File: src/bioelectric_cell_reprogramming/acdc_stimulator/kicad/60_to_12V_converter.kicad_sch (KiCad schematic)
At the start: 7 parts, among them IC4 LTC3637IMSE#PBF

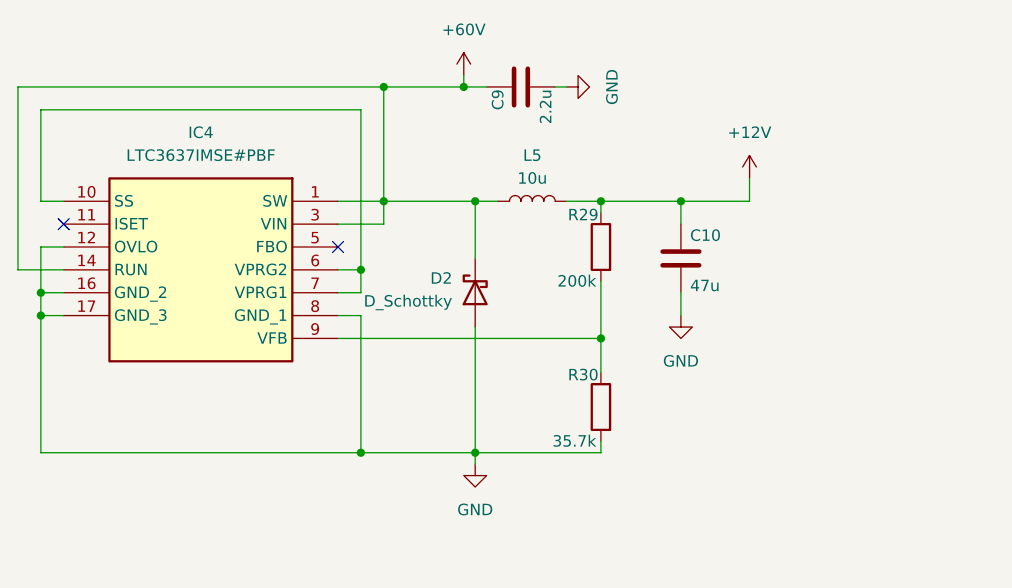
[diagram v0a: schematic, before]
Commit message: CI: footprint assignment done
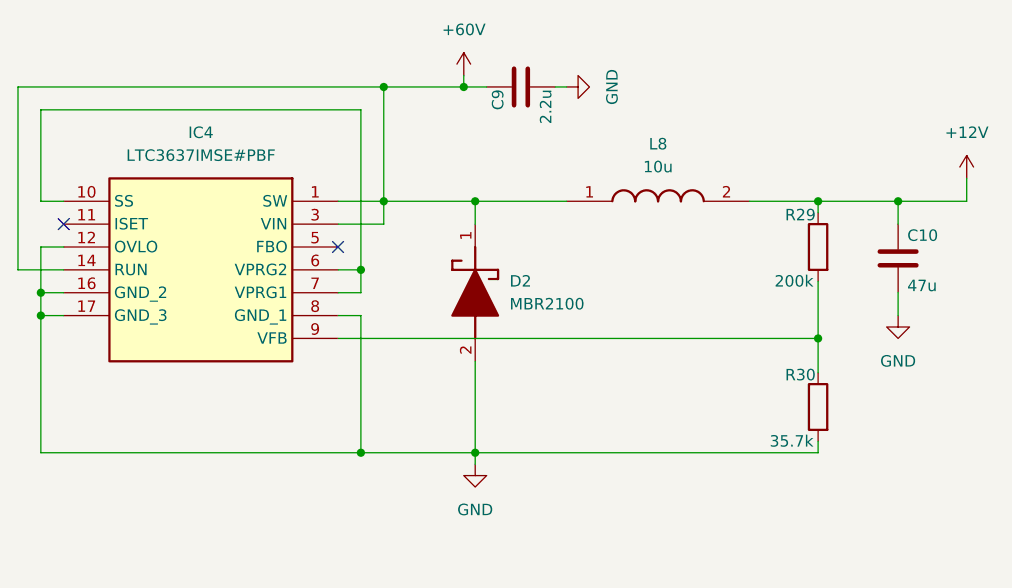
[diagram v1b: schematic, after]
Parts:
- removed D2: D_Schottky, symbol Device:D_Schottky
- removed L5: 10u, symbol Device:L
- added D2: MBR2100, MBR2100:DIOAD1910W86L670D310, symbol MBR2100:MBR2100
- added L8: 10u, SRP1270-100M:INDPM137137X700N, symbol SRP1270-100M:SRP1270-100M
- C10: footprint (none) -> Capacitor_SMD:C_0805_2012Metric
- C9: footprint (none) -> Capacitor_SMD:C_0603_1608Metric
- IC4: footprint LTC3637IMSEPBF -> LTC3637IMSE#PBF:LTC3637IMSEPBF
- R29: footprint (none) -> Resistor_SMD:R_0603_1608Metric
- R30: footprint (none) -> Resistor_SMD:R_0402_1005Metric
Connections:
- net +12V: now also L8.2
- net +60V: now also D2.1 (K), L8.1
- net GND: now also D2.2 (A)
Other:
- moved on the sheet: C10, R29, R30

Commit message: ci: STM32 layout done and schematic annotated
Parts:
- renumbered C9 to C53, C10 to C54, L8 to L5, R29 to R28, R30 to R29
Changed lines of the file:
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@@
 		(dnp no)
 		(fields_autoplaced yes)
-		(property "Reference" "#PWR081"
+		(property "Reference" "#PWR086"
 			(at 179.07 72.39 0)
 			(effects
@@
 			(project "acdc_stimulator"
 				(path "/ec70e9f6-566f-44ea-8141-5580f51beca4/cf0126de-2a37-4fca-bf65-f8dc79cc90bd"
-					(reference "#PWR081")
+					(reference "#PWR086")
 					(unit 1)
 				)
@@
 		(dnp no)
 		(fields_autoplaced yes)
-		(property "Reference" "L8"
+		(property "Reference" "L5"
 			(at 182.88 78.74 0)
 			(effects
@@
 			(project ""
 				(path "/ec70e9f6-566f-44ea-8141-5580f51beca4/cf0126de-2a37-4fca-bf65-f8dc79cc90bd"
-					(reference "L8")
+					(reference "L5")
 					(unit 1)
 				)
@@
 		(on_board yes)
 		(dnp no)
-		(property "Reference" "R30"
+		(property "Reference" "R29"
 			(at 200.406 104.394 0)
 			(effects
@@
 			(project "acdc_stimulator"
 				(path "/ec70e9f6-566f-44ea-8141-5580f51beca4/cf0126de-2a37-4fca-bf65-f8dc79cc90bd"
-					(reference "R30")
+					(reference "R29")
 					(unit 1)
 				)
@@
 		(dnp no)
 		(fields_autoplaced yes)
-		(property "Reference" "#PWR025"
+		(property "Reference" "#PWR084"
 			(at 161.29 74.93 0)
 			(effects
@@
 			(project "acdc_stimulator"
 				(path "/ec70e9f6-566f-44ea-8141-5580f51beca4/cf0126de-2a37-4fca-bf65-f8dc79cc90bd"
-					(reference "#PWR025")
+					(reference "#PWR084")
 					(unit 1)
 				)
@@
 		(on_board yes)
 		(dnp no)
-		(property "Reference" "C10"
+		(property "Reference" "C54"
 			(at 210.566 88.9 0)
 			(effects
@@
 			(project "acdc_stimulator"
 				(path "/ec70e9f6-566f-44ea-8141-5580f51beca4/cf0126de-2a37-4fca-bf65-f8dc79cc90bd"
-					(reference "C10")
+					(reference "C54")
 					(unit 1)
 				)
@@
 		(dnp no)
 		(fields_autoplaced yes)
-		(property "Reference" "#PWR082"
+		(property "Reference" "#PWR087"
 			(at 209.55 104.14 0)
 			(effects
@@
 			(project "acdc_stimulator"
 				(path "/ec70e9f6-566f-44ea-8141-5580f51beca4/cf0126de-2a37-4fca-bf65-f8dc79cc90bd"
-					(reference "#PWR082")
+					(reference "#PWR087")
 					(unit 1)
 				)
@@
 		(on_board yes)
 		(dnp no)
-		(property "Reference" "C9"
+		(property "Reference" "C53"
 			(at 165.1 72.644 0)
 			(effects
@@
 			(project "acdc_stimulator"
 				(path "/ec70e9f6-566f-44ea-8141-5580f51beca4/cf0126de-2a37-4fca-bf65-f8dc79cc90bd"
-					(reference "C9")
+					(reference "C53")
 					(unit 1)
 				)
@@
 		(dnp no)
 		(fields_autoplaced yes)
-		(property "Reference" "#PWR083"
+		(property "Reference" "#PWR088"
 			(at 217.17 86.36 0)
 			(effects
@@
 			(project "acdc_stimulator"
 				(path "/ec70e9f6-566f-44ea-8141-5580f51beca4/cf0126de-2a37-4fca-bf65-f8dc79cc90bd"
-					(reference "#PWR083")
+					(reference "#PWR088")
 					(unit 1)
 				)
@@
 		(on_board yes)
 		(dnp no)
-		(property "Reference" "R29"
+		(property "Reference" "R28"
 			(at 200.406 86.614 0)
 			(effects
@@
 			(project "acdc_stimulator"
 				(path "/ec70e9f6-566f-44ea-8141-5580f51beca4/cf0126de-2a37-4fca-bf65-f8dc79cc90bd"
-					(reference "R29")
+					(reference "R28")
 					(unit 1)
 				)
@@
 		(dnp no)
 		(fields_autoplaced yes)
-		(property "Reference" "#PWR080"
+		(property "Reference" "#PWR085"
 			(at 162.56 120.65 0)
 			(effects
@@
 			(project "acdc_stimulator"
 				(path "/ec70e9f6-566f-44ea-8141-5580f51beca4/cf0126de-2a37-4fca-bf65-f8dc79cc90bd"
-					(reference "#PWR080")
-					(unit 1)
-				)
+					(reference "#PWR085")
+					(unit 1)
+				)

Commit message: ci: layout done
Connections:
- net +60V: no longer D2.1 (K), IC4.1 (SW), L5.1
- new net: D2.1 (K), IC4.1 (SW), L5.1
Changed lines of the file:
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@@
 	(paper "A4")
 	(junction
+		(at 152.4 72.39)
+		(diameter 0)
+		(color 0 0 0 0)
+	)
+	(junction
 		(at 149.86 92.71)
 		(diameter 0)
@@
 	)
 	(junction
-		(at 152.4 72.39)
-		(diameter 0)
-		(color 0 0 0 0)
-	)
-	(junction
 		(at 200.66 100.33)
-		(diameter 0)
-		(color 0 0 0 0)
-	)
-	(junction
-		(at 152.4 85.09)
 		(diameter 0)
 		(color 0 0 0 0)
@@
 	(wire
 		(pts
-			(xy 152.4 85.09) (xy 147.32 85.09)
+			(xy 147.32 85.09) (xy 162.56 85.09)
 		)
 		(stroke
@@
 	(wire
 		(pts
-			(xy 161.29 72.39) (xy 152.4 72.39)
-		)
-		(stroke
-			(width 0)
-			(type default)
-		)
-	)
-	(wire
-		(pts
 			(xy 147.32 97.79) (xy 149.86 97.79)
 		)
@@
 	(wire
 		(pts
-			(xy 152.4 85.09) (xy 152.4 87.63)
-		)
-		(stroke
-			(width 0)
-			(type default)
-		)
-	)
-	(wire
-		(pts
 			(xy 114.3 95.25) (xy 114.3 90.17)
 		)
@@
 	(wire
 		(pts
-			(xy 152.4 85.09) (xy 162.56 85.09)
+			(xy 152.4 72.39) (xy 152.4 87.63)
 		)
 		(stroke
@@
 	(wire
 		(pts
+			(xy 152.4 72.39) (xy 161.29 72.39)
+		)
+		(stroke
+			(width 0)
+			(type default)
+		)
+	)
+	(wire
+		(pts
 			(xy 193.04 85.09) (xy 200.66 85.09)
 		)
@@
 		)
 		(stroke
-			(width 0)
-			(type default)
-		)
-	)
-	(wire
-		(pts
-			(xy 152.4 72.39) (xy 152.4 85.09)
-		)
-		(stroke

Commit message: BOM in progress
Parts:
- C53: Distributor Link (none) -> https://jlcpcb.com/partdetail/3409988-GRM21BD72A225KE01L/C2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; Manufacturer (none) -> Murata Electronics; Manufacturer Part Number (none) -> GRM21BD72A225KE01L
- C54: footprint Capacitor_SMD:C_0805_2012Metric -> Capacitor_SMD:C_1206_3216Metric; Distributor Link (none) -> https://jlcpcb.com/partdetail/183737-1206X476M160NT/C172351; Manufacturer (none) -> FH (Guangdong Fenghua Advanced Tech); Manufacturer Part Number (none) -> 1206X476M160NT
- D2: Distributor Link (none) -> https://www.digikey.com/en/products/detail/panjit-internati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; Manufacturer (none) -> Panjit International Inc.; Manufacturer Part Number (none) -> MBR2100_R2_00001
- IC4: Distributor Link (none) -> https://jlcpcb.com/partdetail/AnalogDevices-LTC3637IMSEPBF/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; Manufacturer (none) -> Analog Devices; Manufacturer Part Number (none) -> LTC3637IMSE#PBF
- L5: Distributor Link (none) -> https://www.mouser.com/ProductDetail/Bourns/SRP1270-100M?qs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; Manufacturer (none) -> Bourns; Manufacturer Part Number (none) -> SRP1270-100M
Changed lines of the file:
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@@
 			)
 		)
-		(property "Distributor Link" ""
+		(property "Distributor Link" "https://www.digikey.com/en/products/detail/panjit-international-inc/MBR2100-R2-00001/15801106"
 			(at 162.56 85.09 0)
 			(effects
@@
 			)
 		)
-		(property "Manufacturer" ""
+		(property "Manufacturer" "Panjit International Inc."
 			(at 162.56 85.09 0)
 			(effects
@@
 			)
 		)
-		(property "Manufacturer Part Number" ""
+		(property "Manufacturer Part Number" "MBR2100_R2_00001"
+			(at 162.56 85.09 0)
+			(effects
+				(font
+					(size 1.27 1.27)
+				)
+				(hide yes)
+			)
+		)
+		(property "JLCPCB Part #" ""
 			(at 162.56 85.09 0)
 			(effects
@@
 			)
 		)
-		(property "Distributor Link" ""
+		(property "Distributor Link" "https://www.mouser.com/ProductDetail/Bourns/SRP1270-100M?qs=s%252BX%2FYkvGCpE5rFNaoMUDIw%3D%3D"
 			(at 172.72 85.09 0)
 			(effects
@@
 			)
 		)
-		(property "Manufacturer" ""
+		(property "Manufacturer" "Bourns"
 			(at 172.72 85.09 0)
 			(effects
@@
 			)
 		)
-		(property "Manufacturer Part Number" ""
+		(property "Manufacturer Part Number" "SRP1270-100M"
+			(at 172.72 85.09 0)
+			(effects
+				(font
+					(size 1.27 1.27)
+				)
+				(hide yes)
+			)
+		)
+		(property "JLCPCB Part #" ""
 			(at 172.72 85.09 0)
 			(effects
@@
 			)
 		)
+		(property "JLCPCB Part #" ""
+			(at 200.66 107.95 0)
+			(effects
+				(font
+					(size 1.27 1.27)
+				)
+				(hide yes)
+			)
+		)
 		(pin "1"
 		)
@@
 			)
 		)
-		(property "Footprint" "Capacitor_SMD:C_0805_2012Metric"
+		(property "Footprint" "Capacitor_SMD:C_1206_3216Metric"
 			(at 210.5152 95.25 0)
 			(effects
@@
 			)
 		)
-		(property "Distributor Link" ""
+		(property "Distributor Link" "https://jlcpcb.com/partdetail/183737-1206X476M160NT/C172351"
 			(at 209.55 91.44 0)
 			(effects
@@
 			)
 		)
-		(property "Manufacturer" ""
+		(property "Manufacturer" "FH (Guangdong Fenghua Advanced Tech)"
 			(at 209.55 91.44 0)
 			(effects
@@
 			)
 		)
-		(property "Manufacturer Part Number" ""
+		(property "Manufacturer Part Number" "1206X476M160NT"
+			(at 209.55 91.44 0)
+			(effects
+				(font
+					(size 1.27 1.27)
+				)
+				(hide yes)
+			)
+		)
+		(property "JLCPCB Part #" ""
 			(at 209.55 91.44 0)
 			(effects
@@
 			)
 		)
-		(property "Distributor Link" ""
+		(property "Distributor Link" "https://jlcpcb.com/partdetail/AnalogDevices-LTC3637IMSEPBF/C580783"
 			(at 147.32 85.09 0)
 			(effects
@@
 			)
 		)
-		(property "Manufacturer" ""
+		(property "Manufacturer" "Analog Devices"
 			(at 147.32 85.09 0)
 			(effects
@@
 			)
 		)
-		(property "Manufacturer Part Number" ""
+		(property "Manufacturer Part Number" "LTC3637IMSE#PBF"
+			(at 147.32 85.09 0)
+			(effects
+				(font
+					(size 1.27 1.27)
+				)
+				(hide yes)
+			)
+		)
+		(property "JLCPCB Part #" ""
 			(at 147.32 85.09 0)
 			(effects
@@
 			)
 		)
-		(property "Distributor Link" ""
+		(property "Distributor Link" "https://jlcpcb.com/partdetail/3409988-GRM21BD72A225KE01L/C2981733"
 			(at 167.64 72.39 0)
 			(effects
@@
 			)
 		)
-		(property "Manufacturer" ""
+		(property "Manufacturer" " Murata Electronics"
 			(at 167.64 72.39 0)
 			(effects
@@
 			)
 		)
-		(property "Manufacturer Part Number" ""
+		(property "Manufacturer Part Number" "GRM21BD72A225KE01L"
+			(at 167.64 72.39 0)
+			(effects
+				(font
+					(size 1.27 1.27)
+				)
+				(hide yes)
+			)
+		)
+		(property "JLCPCB Part #" ""
 			(at 167.64 72.39 0)
 			(effects
@@
 			(at 200.66 90.17 0)
 			(effects
+				(font
+					(size 1.27 1.27)
+				)
+				(hide yes)
+			)
+		)
+		(property "JLCPCB Part #" ""
+			(at 200.66 90.17 0)
+			(effects

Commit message: fixed values for resistive divider of LDOs
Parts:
- L5: Distributor Link https://www.mouser.com/ProductDetail/Bourns/SRP1270-100M?qs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 -> https://jlcpcb.com/partdetail/Bourns-SRP1270100M/C2042024; Manufacturer Bourns -> BOURNS
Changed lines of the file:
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@@
 			)
 		)
-		(property "Distributor Link" "https://www.mouser.com/ProductDetail/Bourns/SRP1270-100M?qs=s%252BX%2FYkvGCpE5rFNaoMUDIw%3D%3D"
+		(property "Distributor Link" "https://jlcpcb.com/partdetail/Bourns-SRP1270100M/C2042024"
 			(at 172.72 85.09 0)
 			(effects
@@
 			)
 		)
-		(property "Manufacturer" "Bourns"
+		(property "Manufacturer" "BOURNS"
 			(at 172.72 85.09 0)
 			(effects

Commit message: ci: BOM done
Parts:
- R28: Distributor Link (none) -> https://jlcpcb.com/partdetail/26554-0603WAF2003T5E/C25811; Manufacturer (none) -> UNI-ROYAL(Uniroyal Elec); Manufacturer Part Number (none) -> 0603WAF2003T5E
- R29: footprint Resistor_SMD:R_0402_1005Metric -> Resistor_SMD:R_0603_1608Metric; Distributor Link (none) -> https://jlcpcb.com/partdetail/23754-0603WAF3572T5E/C23027; Manufacturer (none) -> UNI-ROYAL(Uniroyal Elec); Manufacturer Part Number (none) -> 0603WAF3572T5E
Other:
- note added: "VFB (internal feedback voltage) is 1.8V when both Vprg are tied to SS"
- note added: "Vout = 1.8(1+R1/R2)"
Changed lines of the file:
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@@
+		)
+	)
+	(text "VFB (internal feedback voltage) is 1.8V when both Vprg are tied to SS\n"
+		(exclude_from_sim no)
+		(at 169.672 124.968 0)
+		(effects
+			(font
+				(size 1.27 1.27)
+			)
+		)
+	)
+	(text "Vout = 1.8(1+R1/R2)"
+		(exclude_from_sim no)
+		(at 188.722 98.298 0)
+		(effects
+			(font
+				(size 1.27 1.27)
+			)
 		)
 	)
@@
 			)
 		)
-		(property "Footprint" "Resistor_SMD:R_0402_1005Metric"
+		(property "Footprint" "Resistor_SMD:R_0603_1608Metric"
 			(at 202.438 107.95 90)
 			(effects
@@
 			)
 		)
-		(property "Distributor Link" ""
+		(property "Distributor Link" "https://jlcpcb.com/partdetail/23754-0603WAF3572T5E/C23027"
 			(at 200.66 107.95 0)
 			(effects
@@
 			)
 		)
-		(property "Manufacturer" ""
+		(property "Manufacturer" "UNI-ROYAL(Uniroyal Elec)"
 			(at 200.66 107.95 0)
 			(effects
@@
 			)
 		)
-		(property "Manufacturer Part Number" ""
+		(property "Manufacturer Part Number" "0603WAF3572T5E"
 			(at 200.66 107.95 0)
 			(effects
@@
 			)
 		)
-		(property "Distributor Link" ""
+		(property "Distributor Link" "https://jlcpcb.com/partdetail/26554-0603WAF2003T5E/C25811"
 			(at 200.66 90.17 0)
 			(effects
@@
 			)
 		)
-		(property "Manufacturer" ""
+		(property "Manufacturer" "UNI-ROYAL(Uniroyal Elec)"
 			(at 200.66 90.17 0)
 			(effects
@@
 			)
 		)
-		(property "Manufacturer Part Number" ""
+		(property "Manufacturer Part Number" "0603WAF2003T5E"
 			(at 200.66 90.17 0)
 			(effects

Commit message: ci: build files for v0.0.2 generated
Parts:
- removed D2: MBR2100, MBR2100:DIOAD1910W86L670D310, symbol MBR2100:MBR2100
- removed L5: 10u, SRP1270-100M:INDPM137137X700N, symbol SRP1270-100M:SRP1270-100M
- added D5: B2100AE-13, DIOM5226X240N, symbol B2100AE-13:B2100AE-13
- added L8: 10u, INDPM8080X420N, symbol SWPA8040S100MT:SWPA8040S100MT
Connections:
- net +12V: now also L8.2
- net GND: now also D5.2 (A)
- net at IC4.1 (SW): now also D5.1 (K), L8.1
